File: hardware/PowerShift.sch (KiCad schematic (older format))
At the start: 57 parts, among them J1 Barrel_Jack, J10 SHIFT_OUT, J11 JST-ZR, J12 JST-ZR, J14 JST-ZR, J2 MICRO_USB, J3 JST-ZR, J4 JST-ZR, J5 SHIFT_IN, J6 SHIFT_IN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

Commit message: PDI header to 1.27mm SMD
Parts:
- J7: footprint Pin_Headers:Pin_Header_Straight_2x03_Pitch2.54mm -> kuro:3x2_1.27mm_SMD_header

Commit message: DC jack footprint
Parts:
- J1: footprint (none) -> kuro:DC_Jack_SMD_FC6814xS_6941
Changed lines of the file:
@@
 F 0 "J1" H 800 1260 50  0000 C CNN
 F 1 "Barrel_Jack" H 800 875 50  0000 C CNN
-F 2 "" H 850 1010 50  0001 C CNN
+F 2 "kuro:DC_Jack_SMD_FC6814xS_6941" H 850 1010 50  0001 C CNN
 F 3 "" H 850 1010 50  0001 C CNN
 	1    800  1050

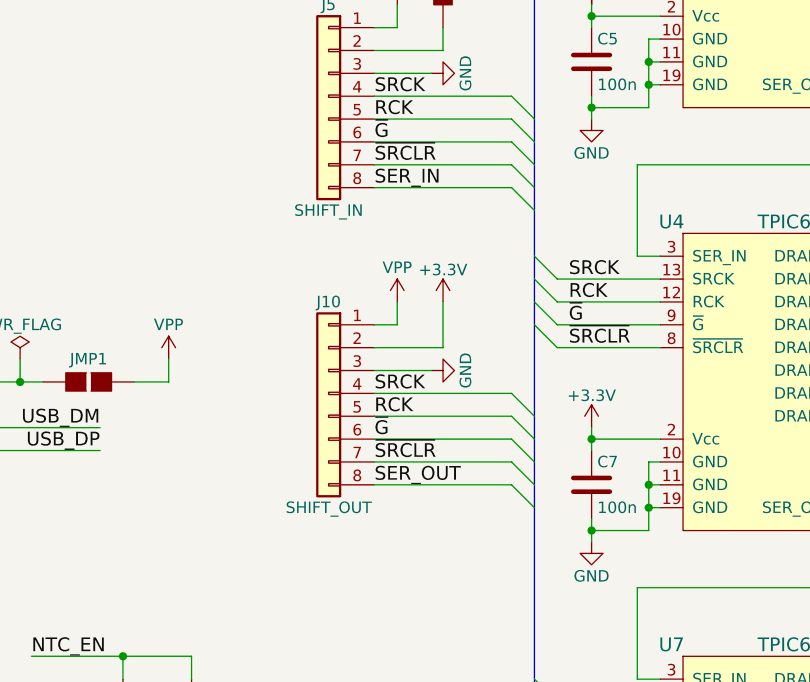
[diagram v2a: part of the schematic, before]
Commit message: Combined in/out header
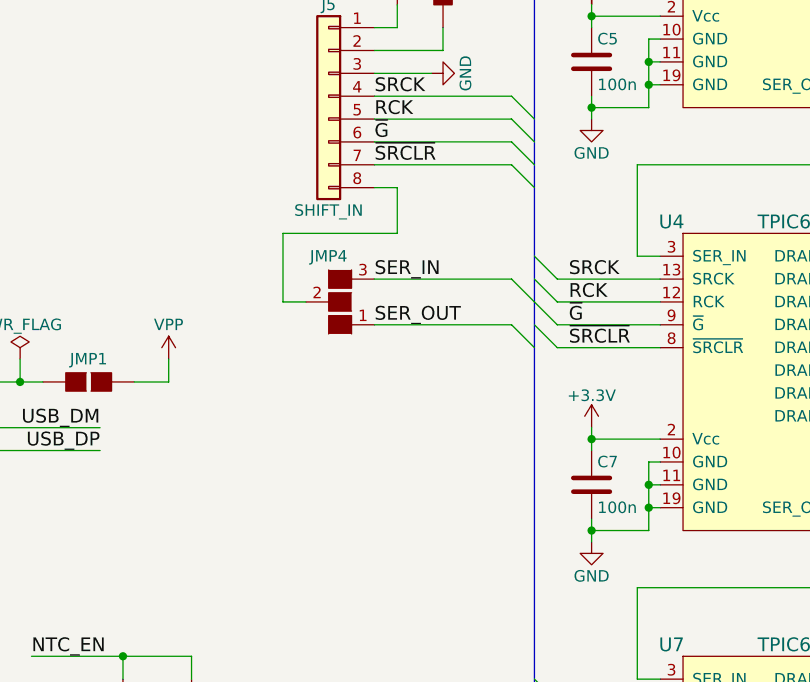
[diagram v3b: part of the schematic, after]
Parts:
- removed J10: SHIFT_OUT, kuro:B8B-ZR-SM4-TF, symbol Conn_01x08
- added JMP4: GS3, Connectors:GS3, symbol GS3
- J5: footprint kuro:B8B-ZR-SM4-TF -> Pin_Headers:Pin_Header_Straight_1x08_Pitch2.54mm
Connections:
- net SER_IN: now also JMP4.3 (G3); no longer J5.8 (Pin_8)
- net SER_OUT: now also JMP4.1 (G1)
- new net: J5.8 (Pin_8), JMP4.2 (G2)
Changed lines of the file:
@@
 	9500 700  8950 700
-$Comp
-L Conn_01x08 J10
-U 1 1 5B307863
-P 5900 3350
-F 0 "J10" H 5900 3750 50  0000 C CNN
-F 1 "SHIFT_OUT" H 5900 2850 50  0000 C CNN
-F 2 "kuro:B8B-ZR-SM4-TF" H 5900 3350 50  0001 C CNN
-F 3 "" H 5900 3350 50  0001 C CNN
-	1    5900 3350
-	-1   0    0    -1
-$EndComp
 $Comp
 L GS2 JMP1
@@
 Wire Wire Line
 	700  2900 1200 2900
-$Comp
-L VPP #PWR026
-U 1 1 5B30B3A1
-P 6200 2950
-F 0 "#PWR026" H 6200 2800 50  0001 C CNN
-F 1 "VPP" H 6200 3100 50  0000 C CNN
-F 2 "" H 6200 2950 50  0001 C CNN
-F 3 "" H 6200 2950 50  0001 C CNN
-	1    6200 2950
-	1    0    0    -1
-$EndComp
-$Comp
-L +3.3V #PWR027
-U 1 1 5B30B4F6
-P 6400 2950
-F 0 "#PWR027" H 6400 2800 50  0001 C CNN
-F 1 "+3.3V" H 6400 3090 50  0000 C CNN
-F 2 "" H 6400 2950 50  0001 C CNN
-F 3 "" H 6400 2950 50  0001 C CNN
-	1    6400 2950
-	1    0    0    -1
-$EndComp
-$Comp
-L GND #PWR028
-U 1 1 5B30B55B
-P 6350 3250
-F 0 "#PWR028" H 6350 3000 50  0001 C CNN
-F 1 "GND" H 6350 3100 50  0000 C CNN
-F 2 "" H 6350 3250 50  0001 C CNN
-F 3 "" H 6350 3250 50  0001 C CNN
-	1    6350 3250
-	0    -1   -1   0
-$EndComp
-Wire Wire Line
-	6100 3050 6200 3050
-Wire Wire Line
-	6200 3050 6200 2950
-Wire Wire Line
-	6100 3150 6400 3150
-Wire Wire Line
-	6400 3150 6400 2950
-Entry Wire Line
-	6700 3650 6800 3750
-Entry Wire Line
-	6700 3550 6800 3650
-Entry Wire Line
-	6700 3450 6800 3550
-Entry Wire Line
-	6700 3350 6800 3450
-Wire Wire Line
-	6100 3350 6700 3350
-Wire Wire Line
-	6100 3450 6700 3450
-Wire Wire Line
-	6100 3550 6700 3550
-Wire Wire Line
-	6100 3650 6700 3650
-Wire Wire Line
-	6100 3250 6350 3250
 Wire Wire Line
 	10500 5700 11000 5700
@@
 F 0 "J5" H 5900 2450 50  0000 C CNN
 F 1 "SHIFT_IN" H 5900 1550 50  0000 C CNN
-F 2 "kuro:B8B-ZR-SM4-TF" H 5900 2050 50  0001 C CNN
+F 2 "Pin_Headers:Pin_Header_Straight_1x08_Pitch2.54mm" H 5900 2050 50  0001 C CNN
 F 3 "" H 5900 2050 50  0001 C CNN
 	1    5900 2050
@@
 	6700 2350 6800 2450
 Entry Wire Line
-	6700 2450 6800 2550
+	6700 2850 6800 2950
 Wire Wire Line
 	6100 2050 6700 2050
@@
 Wire Wire Line
 	6100 2350 6700 2350
-Wire Wire Line
-	6100 2450 6700 2450
 $Comp
 L GS2 JMP2
@@
 Text Label 10600 5700 0    60   ~ 0
 SER_OUT
-Text Label 6100 3350 0    60   ~ 0
-SRCK
-Text Label 6100 3450 0    60   ~ 0
-RCK
-Text Label 6100 3550 0    60   ~ 0
-~G
-Text Label 6100 3650 0    60   ~ 0
-~SRCLR
 Text Label 6100 2050 0    60   ~ 0
 SRCK
@@
 Text Label 6100 2350 0    60   ~ 0
 ~SRCLR
-Text Label 6100 2450 0    60   ~ 0
+Text Label 6100 2850 0    60   ~ 0
 SER_IN
 Text Label 5350 6650 2    60   ~ 0
@@
 Wire Wire Line
 	11000 6200 11000 5700
-Text Label 6100 3750 0    60   ~ 0
+Text Label 6100 3050 0    60   ~ 0
 SER_OUT
 Entry Wire Line
-	6700 3750 6800 3850
-Wire Wire Line
-	6100 3750 6700 3750
+	6700 3050 6800 3150
 NoConn ~ 8250 1800
 NoConn ~ 8250 1900
@@
 	-400 4000 -400 4050
 Connection ~ -750 4000
+$Comp
+L GS3 JMP4
+U 1 1 5B32F30E
+P 5950 2950
+F 0 "JMP4" H 6000 2750 50  0000 C CNN
+F 1 "GS3" H 6000 2751 50  0001 C CNN
+F 2 "Connectors:GS3" V 6038 2876 50  0001 C CNN
+F 3 "" H 5950 2950 50  0001 C CNN
+	1    5950 2950
+	-1   0    0    1
+$EndComp
+Wire Wire Line
+	6100 3050 6700 3050
+Wire Wire Line
+	6700 2850 6100 2850
+Wire Wire Line
+	6100 2450 6200 2450
+Wire Wire Line
+	6200 2450 6200 2650
+Wire Wire Line
+	6200 2650 5700 2650
+Wire Wire Line
+	5700 2650 5700 2950
+Wire Wire Line
+	5700 2950 5800 2950
 $EndSCHEMATC

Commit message: Mounting holes
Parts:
- added M? (x4): TEST, Mounting_Holes:MountingHole_2.7mm_M2.5_Pad, symbol TEST
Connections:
- net GND: now also M?.1, M?.1, M?.1, M?.1
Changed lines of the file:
@@
 $EndComp
 $Comp
-L VPP #PWR029
+L VPP #PWR026
 U 1 1 5B30E650
 P 6200 1650
-F 0 "#PWR029" H 6200 1500 50  0001 C CNN
+F 0 "#PWR026" H 6200 1500 50  0001 C CNN
 F 1 "VPP" H 6200 1800 50  0000 C CNN
 F 2 "" H 6200 1650 50  0001 C CNN
@@
 $EndComp
 $Comp
-L +3.3V #PWR030
+L +3.3V #PWR027
 U 1 1 5B30E656
 P 6400 1250
-F 0 "#PWR030" H 6400 1100 50  0001 C CNN
+F 0 "#PWR027" H 6400 1100 50  0001 C CNN
 F 1 "+3.3V" H 6400 1390 50  0000 C CNN
 F 2 "" H 6400 1250 50  0001 C CNN
@@
 $EndComp
 $Comp
-L GND #PWR031
+L GND #PWR028
 U 1 1 5B30E65C
 P 6350 1950
-F 0 "#PWR031" H 6350 1700 50  0001 C CNN
+F 0 "#PWR028" H 6350 1700 50  0001 C CNN
 F 1 "GND" H 6350 1800 50  0000 C CNN
 F 2 "" H 6350 1950 50  0001 C CNN
@@
 ~G
 $Comp
-L +3.3V #PWR032
+L +3.3V #PWR029
 U 1 1 5B312626
 P 7050 1650
-F 0 "#PWR032" H 7050 1500 50  0001 C CNN
+F 0 "#PWR029" H 7050 1500 50  0001 C CNN
 F 1 "+3.3V" H 7050 1790 50  0000 C CNN
 F 2 "" H 7050 1650 50  0001 C CNN
@@
 ~G
 $Comp
-L +3.3V #PWR033
+L +3.3V #PWR030
 U 1 1 5B31298E
 P 9300 5350
-F 0 "#PWR033" H 9300 5200 50  0001 C CNN
+F 0 "#PWR030" H 9300 5200 50  0001 C CNN
 F 1 "+3.3V" H 9300 5490 50  0000 C CNN
 F 2 "" H 9300 5350 50  0001 C CNN
@@
 ~G
 $Comp
-L +3.3V #PWR034
+L +3.3V #PWR031
 U 1 1 5B3129BE
 P 9300 3500
-F 0 "#PWR034" H 9300 3350 50  0001 C CNN
+F 0 "#PWR031" H 9300 3350 50  0001 C CNN
 F 1 "+3.3V" H 9300 3640 50  0000 C CNN
 F 2 "" H 9300 3500 50  0001 C CNN
@@
 ~G
 $Comp
-L +3.3V #PWR035
+L +3.3V #PWR032
 U 1 1 5B312AAE
 P 9300 1650
-F 0 "#PWR035" H 9300 1500 50  0001 C CNN
+F 0 "#PWR032" H 9300 1500 50  0001 C CNN
 F 1 "+3.3V" H 9300 1790 50  0000 C CNN
 F 2 "" H 9300 1650 50  0001 C CNN
@@
 $EndComp
 $Comp
-L +3.3V #PWR036
+L +3.3V #PWR033
 U 1 1 5B317FE8
 P 650 4350
-F 0 "#PWR036" H 650 4200 50  0001 C CNN
+F 0 "#PWR033" H 650 4200 50  0001 C CNN
 F 1 "+3.3V" H 650 4490 50  0000 C CNN
 F 2 "" H 650 4350 50  0001 C CNN
@@
 $EndComp
 $Comp
-L GND #PWR037
+L GND #PWR034
 U 1 1 5B318098
 P 650 4850
-F 0 "#PWR037" H 650 4600 50  0001 C CNN
+F 0 "#PWR034" H 650 4600 50  0001 C CNN
 F 1 "GND" H 650 4700 50  0000 C CNN
 F 2 "" H 650 4850 50  0001 C CNN
@@
 Connection ~ 1100 6450
 $Comp
-L GND #PWR038
+L GND #PWR035
 U 1 1 5B3198CA
 P 1100 6550
-F 0 "#PWR038" H 1100 6300 50  0001 C CNN
+F 0 "#PWR035" H 1100 6300 50  0001 C CNN
 F 1 "GND" H 1100 6400 50  0000 C CNN
 F 2 "" H 1100 6550 50  0001 C CNN
@@
 	4850 5450 5800 5450
 $Comp
-L GND #PWR039
+L GND #PWR036
 U 1 1 5B31C53F
 P 5000 5000
-F 0 "#PWR039" H 5000 4750 50  0001 C CNN
+F 0 "#PWR036" H 5000 4750 50  0001 C CNN
 F 1 "GND" H 5000 4850 50  0000 C CNN
 F 2 "" H 5000 5000 50  0001 C CNN
@@
 Connection ~ 5300 5450
 $Comp
-L GND #PWR040
+L GND #PWR037
 U 1 1 5B31CE60
 P 5700 5650
-F 0 "#PWR040" H 5700 5400 50  0001 C CNN
+F 0 "#PWR037" H 5700 5400 50  0001 C CNN
 F 1 "GND" H 5700 5500 50  0000 C CNN
 F 2 "" H 5700 5650 50  0001 C CNN
@@
 	-1300 2800 -1300 2750
 $Comp
-L +3.3V #PWR041
+L +3.3V #PWR038
 U 1 1 5B320992
 P -1550 2350
-F 0 "#PWR041" H -1550 2200 50  0001 C CNN
+F 0 "#PWR038" H -1550 2200 50  0001 C CNN
 F 1 "+3.3V" H -1550 2490 50  0000 C CNN
 F 2 "" H -1550 2350 50  0001 C CNN
@@
 Connection ~ -1550 2400
 $Comp
-L +3.3V #PWR042
+L +3.3V #PWR039
 U 1 1 5B3217D3
 P -900 2650
-F 0 "#PWR042" H -900 2500 50  0001 C CNN
+F 0 "#PWR039" H -900 2500 50  0001 C CNN
 F 1 "+3.3V" H -900 2790 50  0000 C CNN
 F 2 "" H -900 2650 50  0001 C CNN
@@
 	-900 2700 -600 2700
 $Comp
-L GND #PWR043
+L GND #PWR040
 U 1 1 5B321D60
 P -700 3400
-F 0 "#PWR043" H -700 3150 50  0001 C CNN
+F 0 "#PWR040" H -700 3150 50  0001 C CNN
 F 1 "GND" H -700 3250 50  0000 C CNN
 F 2 "" H -700 3400 50  0001 C CNN
@@
 	1500 7400 1500 7450
 $Comp
-L GND #PWR044
+L GND #PWR041
 U 1 1 5B326D09
 P 1500 7450
-F 0 "#PWR044" H 1500 7200 50  0001 C CNN
+F 0 "#PWR041" H 1500 7200 50  0001 C CNN
 F 1 "GND" H 1500 7300 50  0000 C CNN
 F 2 "" H 1500 7450 50  0001 C CNN
@@
 	1800 6650 2200 6650
 $Comp
-L VPP #PWR045
+L VPP #PWR042
 U 1 1 5B3369E9
 P -700 2500
-F 0 "#PWR045" H -700 2350 50  0001 C CNN
+F 0 "#PWR042" H -700 2350 50  0001 C CNN
 F 1 "VPP" H -700 2650 50  0000 C CNN
 F 2 "" H -700 2500 50  0001 C CNN
@@
 $EndComp
 $Comp
-L +3.3V #PWR046
+L +3.3V #PWR043
 U 1 1 5B345AFF
 P 5700 5050
-F 0 "#PWR046" H 5700 4900 50  0001 C CNN
+F 0 "#PWR043" H 5700 4900 50  0001 C CNN
 F 1 "+3.3V" H 5700 5190 50  0000 C CNN
 F 2 "" H 5700 5050 50  0001 C CNN
@@
 	5700 5550 5700 5650
 $Comp
-L VPP #PWR047
+L VPP #PWR044
 U 1 1 5B34FA15
 P 3100 3300
-F 0 "#PWR047" H 3100 3150 50  0001 C CNN
+F 0 "#PWR044" H 3100 3150 50  0001 C CNN
 F 1 "VPP" H 3100 3450 50  0000 C CNN
 F 2 "" H 3100 3300 50  0001 C CNN
@@
 $EndComp
 $Comp
-L GND #PWR048
+L GND #PWR045
 U 1 1 5B34FB3F
 P 3400 3350
-F 0 "#PWR048" H 3400 3100 50  0001 C CNN
+F 0 "#PWR045" H 3400 3100 50  0001 C CNN
 F 1 "GND" H 3400 3200 50  0000 C CNN
 F 2 "" H 3400 3350 50  0001 C CNN
@@
 $EndComp
 $Comp
-L PWR_FLAG #FLG049
+L PWR_FLAG #FLG046
 U 1 1 5B34FBA8
 P 3100 3350
-F 0 "#FLG049" H 3100 3425 50  0001 C CNN
+F 0 "#FLG046" H 3100 3425 50  0001 C CNN
 F 1 "PWR_FLAG" H 3100 3500 50  0000 C CNN
 F 2 "" H 3100 3350 50  0001 C CNN
@@
 $EndComp
 $Comp
-L PWR_FLAG #FLG050
+L PWR_FLAG #FLG047
 U 1 1 5B34FCA0
 P 4550 3200
-F 0 "#FLG050" H 4550 3275 50  0001 C CNN
+F 0 "#FLG047" H 4550 3275 50  0001 C CNN
 F 1 "PWR_FLAG" H 4550 3350 50  0000 C CNN
 F 2 "" H 4550 3200 50  0001 C CNN
@@
 $EndComp
 $Comp
-L PWR_FLAG #FLG051
+L PWR_FLAG #FLG048
 U 1 1 5B34FD35
 P 3400 3300
-F 0 "#FLG051" H 3400 3375 50  0001 C CNN
+F 0 "#FLG048" H 3400 3375 50  0001 C CNN
 F 1 "PWR_FLAG" H 3400 3450 50  0000 C CNN
 F 2 "" H 3400 3300 50  0001 C CNN
@@
 Connection ~ 4250 1250
 $Comp
-L GND #PWR052
+L GND #PWR049
 U 1 1 5B319895
 P 3850 2050
-F 0 "#PWR052" H 3850 1800 50  0001 C CNN
+F 0 "#PWR049" H 3850 1800 50  0001 C CNN
 F 1 "GND" H 3850 1900 50  0000 C CNN
 F 2 "" H 3850 2050 50  0001 C CNN
@@
 	3850 2050 3850 2000
 $Comp
-L GND #PWR053
+L GND #PWR050
 U 1 1 5B319B94
 P 4250 1650
-F 0 "#PWR053" H 4250 1400 50  0001 C CNN
+F 0 "#PWR050" H 4250 1400 50  0001 C CNN
 F 1 "GND" H 4250 1500 50  0000 C CNN
 F 2 "" H 4250 1650 50  0001 C CNN
@@
 $EndComp
 $Comp
-L VPP #PWR054
+L VPP #PWR051
 U 1 1 5B31811F
 P 1700 700
-F 0 "#PWR054" H 1700 550 50  0001 C CNN
+F 0 "#PWR051" H 1700 550 50  0001 C CNN
 F 1 "VPP" H 1700 850 50  0000 C CNN
 F 2 "" H 1700 700 50  0001 C CNN
@@
 $EndComp
 $Comp
-L +3.3V #PWR055
+L +3.3V #PWR052
 U 1 1 5B3203F8
 P -750 3950
-F 0 "#PWR055" H -750 3800 50  0001 C CNN
+F 0 "#PWR052" H -750 3800 50  0001 C CNN
 F 1 "+3.3V" H -750 4090 50  0000 C CNN
 F 2 "" H -750 3950 50  0001 C CNN
@@
 $EndComp
 $Comp
-L GND #PWR056
+L GND #PWR053
 U 1 1 5B320563
 P -750 4450
-F 0 "#PWR056" H -750 4200 50  0001 C CNN
+F 0 "#PWR053" H -750 4200 50  0001 C CNN
 F 1 "GND" H -750 4300 50  0000 C CNN
 F 2 "" H -750 4450 50  0001 C CNN
@@
 Wire Wire Line
 	5700 2950 5800 2950
+$Comp
+L TEST M?
+U 1 1 5B335191
+P -750 5150
+F 0 "M?" H -750 5400 50  0000 C BNN
+F 1 "TEST" H -750 5400 50  0001 C CNN
+F 2 "Mounting_Holes:MountingHole_2.7mm_M2.5_Pad" H -750 5150 50  0001 C CNN
+F 3 "" H -750 5150 50  0001 C CNN
+	1    -750 5150
+	1    0    0    -1
+$EndComp
+$Comp
+L TEST M?
+U 1 1 5B3358B4
+P -600 5150
+F 0 "M?" H -600 5400 50  0000 C BNN
+F 1 "TEST" H -600 5400 50  0001 C CNN
+F 2 "Mounting_Holes:MountingHole_2.7mm_M2.5_Pad" H -600 5150 50  0001 C CNN
+F 3 "" H -600 5150 50  0001 C CNN
+	1    -600 5150
+	1    0    0    -1
+$EndComp
+$Comp
+L TEST M?
+U 1 1 5B335977
+P -450 5150
+F 0 "M?" H -450 5400 50  0000 C BNN
+F 1 "TEST" H -450 5400 50  0001 C CNN
+F 2 "Mounting_Holes:MountingHole_2.7mm_M2.5_Pad" H -450 5150 50  0001 C CNN
+F 3 "" H -450 5150 50  0001 C CNN
+	1    -450 5150
+	1    0    0    -1
+$EndComp
+$Comp
+L TEST M?
+U 1 1 5B335A3D
+P -300 5150
+F 0 "M?" H -300 5400 50  0000 C BNN
+F 1 "TEST" H -300 5400 50  0001 C CNN
+F 2 "Mounting_Holes:MountingHole_2.7mm_M2.5_Pad" H -300 5150 50  0001 C CNN
+F 3 "" H -300 5150 50  0001 C CNN
+	1    -300 5150
+	1    0    0    -1
+$EndComp
+$Comp
+L GND #PWR?
+U 1 1 5B335B06
+P -750 5250
+F 0 "#PWR?" H -750 5000 50  0001 C CNN
+F 1 "GND" H -750 5100 50  0000 C CNN
+F 2 "" H -750 5250 50  0001 C CNN
+F 3 "" H -750 5250 50  0001 C CNN
+	1    -750 5250
+	1    0    0    -1
+$EndComp
+Wire Wire Line
+	-750 5150 -750 5250
+Wire Wire Line
+	-750 5200 -300 5200
+Wire Wire Line
+	-600 5200 -600 5150
+Connection ~ -750 5200
+Wire Wire Line
+	-450 5200 -450 5150
+Connection ~ -600 5200
+Wire Wire Line
+	-300 5200 -300 5150
+Connection ~ -450 5200
 $EndSCHEMATC

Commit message: Display power header
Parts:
- added J10: SHIFT_IN, kuro:B8B-ZR-SM4-TF, symbol Conn_01x08
- gave numbers to parts that had none: 4
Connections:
- net VPP: now also J10.1 (Pin_1), J10.2 (Pin_2), J10.3 (Pin_3), J10.4 (Pin_4), J10.5 (Pin_5), J10.6 (Pin_6), J10.7 (Pin_7), J10.8 (Pin_8)

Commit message: R/A PDI header footprint
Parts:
- J7: footprint kuro:3x2_1.27mm_SMD_header -> Pin_Headers:Pin_Header_Angled_2x03_Pitch2.54mm

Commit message: Buttons
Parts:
- added SW1, SW2: SW_Push, kuro:Switch_FSM-JSM-Series, symbol SW_Push
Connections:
- net GND: now also SW1.1, SW2.1
- net BTN1: now reaches U9.10 (AC1OUT/IN0/MISO/RXD0/~OC4DLS~/OC4C/PC6)
- net BTN1: now also SW1.2
- net BTN2: now reaches U9.13 (IN3/TXD0/OC4BHS/OC4D/PC3)
- net BTN2: now also SW2.2
- no-connect marks 22 -> 20
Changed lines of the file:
@@
 NoConn ~ 4850 5850
 NoConn ~ 4850 5950
-NoConn ~ 4850 6450
 NoConn ~ 4850 6550
 Entry Wire Line
@@
 	1800 4500 1800 5950
 Connection ~ 1800 5950
-NoConn ~ 4850 6750
 Text Label 1800 6750 0    60   ~ 0
 RX
@@
 Wire Wire Line
 	-550 6400 -500 6400
+$Comp
+L SW_Push SW1
+U 1 1 5B34B57E
+P -1900 4250
+F 0 "SW1" H -1850 4350 50  0000 L CNN
+F 1 "SW_Push" H -1900 4190 50  0001 C CNN
+F 2 "kuro:Switch_FSM-JSM-Series" H -1900 4450 50  0001 C CNN
+F 3 "" H -1900 4450 50  0001 C CNN
+	1    -1900 4250
+	1    0    0    -1
+$EndComp
+$Comp
+L SW_Push SW2
+U 1 1 5B34B936
+P -1900 4450
+F 0 "SW2" H -1850 4550 50  0000 L CNN
+F 1 "SW_Push" H -1900 4390 50  0001 C CNN
+F 2 "kuro:Switch_FSM-JSM-Series" H -1900 4650 50  0001 C CNN
+F 3 "" H -1900 4650 50  0001 C CNN
+	1    -1900 4450
+	1    0    0    -1
+$EndComp
+$Comp
+L GND #PWR056
+U 1 1 5B34BA0A
+P -2150 4500
+F 0 "#PWR056" H -2150 4250 50  0001 C CNN
+F 1 "GND" H -2150 4350 50  0000 C CNN
+F 2 "" H -2150 4500 50  0001 C CNN
+F 3 "" H -2150 4500 50  0001 C CNN
+	1    -2150 4500
+	1    0    0    -1
+$EndComp
+Wire Wire Line
+	-2100 4250 -2150 4250
+Wire Wire Line
+	-2150 4250 -2150 4500
+Wire Wire Line
+	-2100 4450 -2150 4450
+Connection ~ -2150 4450
+Text Label -1400 4250 2    60   ~ 0
+BTN1
+Text Label -1400 4450 2    60   ~ 0
+BTN2
+Wire Wire Line
+	-1400 4450 -1700 4450
+Wire Wire Line
+	-1700 4250 -1400 4250
+Text Label 5350 6450 2    60   ~ 0
+BTN2
+Text Label 5350 6750 2    60   ~ 0
+BTN1
+Wire Wire Line
+	4850 6450 5350 6450
+Wire Wire Line
+	5350 6750 4850 6750
 $EndSCHEMATC

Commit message: Multi footprint crystal
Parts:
- Y1: footprint kuro:SMD_Crystal_Multi_QC6CB_7A_ABM7 -> kuro:Crystal_2pin_6x3.5_3.2x1.5_Multi
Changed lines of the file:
@@
 F 0 "Y1" H 1100 6100 50  0000 C CNN
 F 1 "Crystal" H 1100 5800 50  0000 C CNN
-F 2 "kuro:SMD_Crystal_Multi_QC6CB_7A_ABM7" H 1100 5950 50  0001 C CNN
+F 2 "kuro:Crystal_2pin_6x3.5_3.2x1.5_Multi" H 1100 5950 50  0001 C CNN
 F 3 "" H 1100 5950 50  0001 C CNN
 	1    1100 5950
